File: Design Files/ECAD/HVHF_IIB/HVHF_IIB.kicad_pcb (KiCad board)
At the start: 2 copper layers, 36 parts, among them J1 1984963, J2 1984963, Q1 PNP, Q2 BFP196E6327HTSA1, T1 BFU590G, T1 NPN

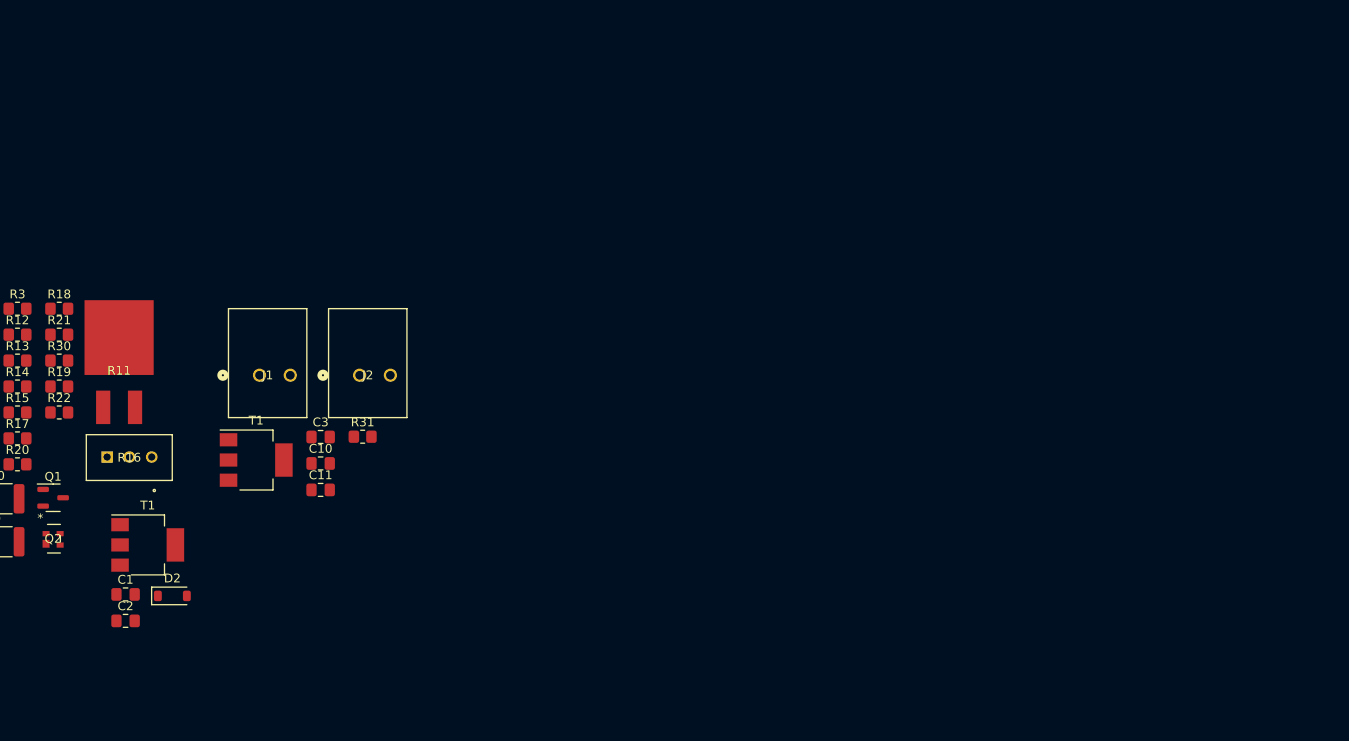
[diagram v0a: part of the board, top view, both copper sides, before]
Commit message: adds footprints
3d models
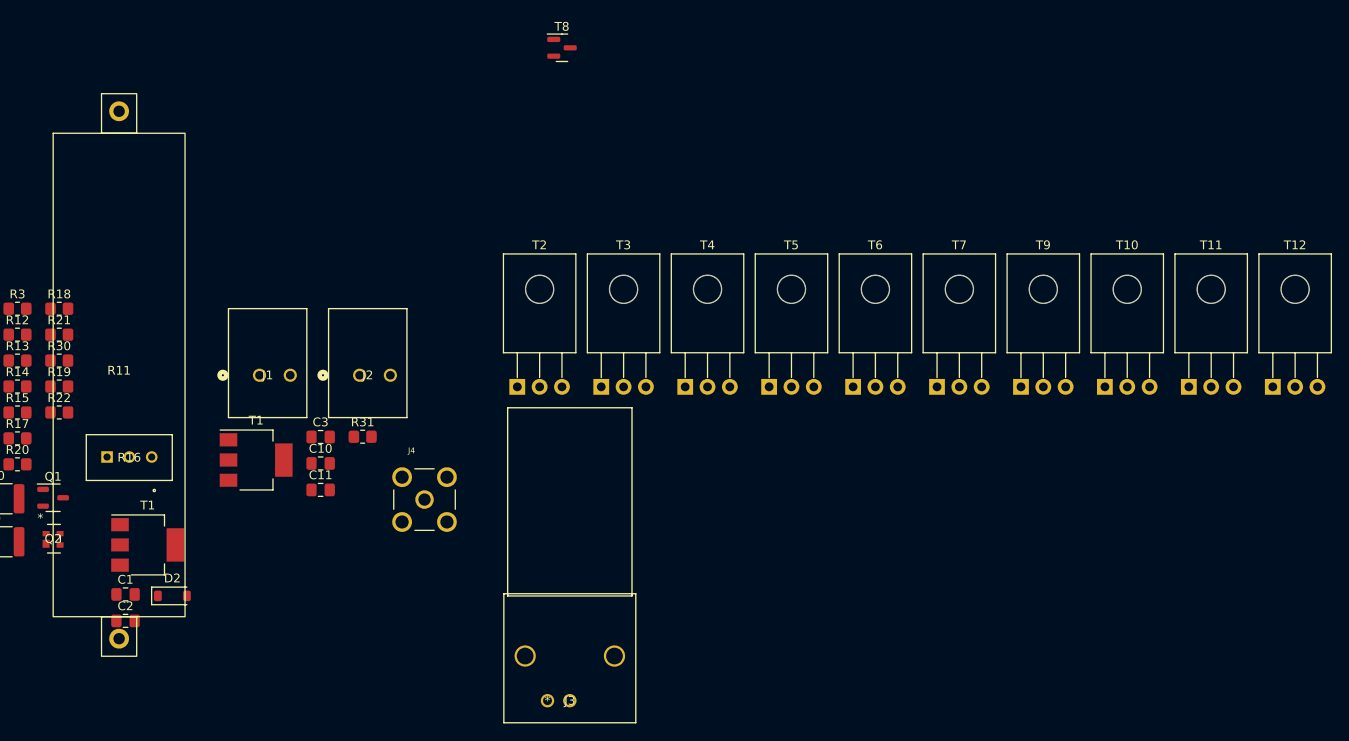
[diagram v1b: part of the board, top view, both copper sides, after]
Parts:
- added J3: 731375003, Library:CONN_73137-5003_MOL, F.Cu at (-298.4, 79.8)
- added J4: CONSMA002-L, Library:LINX_CONSMA002-L, F.Cu at (-314.9, 57.0)
- added T10: BFQ252, Package_TO_SOT_THT:TO-126-3_Horizontal_TabDown, F.Cu at (-237.5, 44.1)
- added T11: BFQ252, Package_TO_SOT_THT:TO-126-3_Horizontal_TabDown, F.Cu at (-228.0, 44.1)
- added T12: BFQ252, Package_TO_SOT_THT:TO-126-3_Horizontal_TabDown, F.Cu at (-218.4, 44.1)
- added T2: BFQ262, Package_TO_SOT_THT:TO-126-3_Horizontal_TabDown, F.Cu at (-304.4, 44.1)
- added T3: BFQ262, Package_TO_SOT_THT:TO-126-3_Horizontal_TabDown, F.Cu at (-294.8, 44.1)
- added T4: BFQ252, Package_TO_SOT_THT:TO-126-3_Horizontal_TabDown, F.Cu at (-285.3, 44.1)
- added T5: BFQ262, Package_TO_SOT_THT:TO-126-3_Horizontal_TabDown, F.Cu at (-275.7, 44.1)
- added T6: BFQ262, Package_TO_SOT_THT:TO-126-3_Horizontal_TabDown, F.Cu at (-266.2, 44.1)
- added T7: BFQ262, Package_TO_SOT_THT:TO-126-3_Horizontal_TabDown, F.Cu at (-256.6, 44.1)
- added T8: ~, Package_TO_SOT_SMD:SOT-23, F.Cu at (-299.3, 5.55)
- added T9: BFQ262, Package_TO_SOT_THT:TO-126-3_Horizontal_TabDown, F.Cu at (-247.1, 44.1)
- R11: footprint Library:PWR163 DPAK -> Library:PWWR0016
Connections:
- J1 pad 1: unconnected-(J1-Pad1) -> +VDC
- J1 pad 2: unconnected-(J1-Pad2) -> GND
- J2 pad 1: unconnected-(J2-Pad1) -> +5V
- J2 pad 2: unconnected-(J2-Pad2) -> GND

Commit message: wrapped up schematic
placed and routed all components on schematic
adds all footprints
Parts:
- added C4: C_Trim, Library:PPZC80003, F.Cu at (142.6, 96.2)
- added C5: 100u, Capacitor_SMD:C_1206_3216Metric_Pad1.33x1.80mm_HandSolder, F.Cu at (153.1, 107.9)
- added C6: 100u, Library:CAP_EEUED_125X25_PAN, F.Cu at (156.2, 99.0)
- added C7: 0.1u, Capacitor_SMD:C_1206_3216Metric_Pad1.33x1.80mm_HandSolder, F.Cu at (153.1, 111.2)
- added D1: BAT64, Library:CR_BAS70-02V_INF-L, F.Cu at (180.8, 104.0)
- added HS1: ~, Library:ATS_PCB1025, F.Cu at (201.8, 94.0)
- added HS10: ~, Library:ATS_PCB1025, F.Cu at (220.0, 127.0)
- added HS2: ~, Library:ATS_PCB1025, F.Cu at (201.8, 105.0)
- added HS3: ~, Library:ATS_PCB1025, F.Cu at (201.8, 116.2)
- added HS4: ~, Library:ATS_PCB1025, F.Cu at (201.8, 127.2)
- added HS5: ~, Library:ATS_PCB1025, F.Cu at (220.0, 71.5)
- added HS6: ~, Library:ATS_PCB1025, F.Cu at (220.0, 82.6)
- added HS7: ~, Library:ATS_PCB1025, F.Cu at (220.0, 93.7)
- added HS8: ~, Library:ATS_PCB1025, F.Cu at (220.0, 104.8)
- added HS9: ~, Library:ATS_PCB1025, F.Cu at (220.0, 115.9)
- moved C1 420.2 mm to (69.5, 105.7)
- moved C10 420.2 mm to (91.7, 90.8)
- moved C11 420.2 mm to (91.7, 93.8)
- moved C2 420.2 mm to (69.5, 108.8)
- moved C3 420.2 mm to (91.7, 87.8)
- moved D2 420.2 mm to (74.9, 105.9)
- moved J1 420.2 mm to (86.6, 80.8)
- moved J2 420.2 mm to (98.0, 80.8)
- moved J4 420.2 mm to (103.5, 95.0)
- moved Q1 420.2 mm to (61.3, 94.7)
- moved Q2 420.2 mm to (61.3, 99.4)
- moved R1 420.2 mm to (52.5, 73.2)
- moved R10 420.2 mm to (54.5, 94.9)
- moved R11 420.2 mm to (68.8, 80.8)
- moved R12 420.2 mm to (57.2, 76.2)
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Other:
- board outline added: 200 x 100 mm

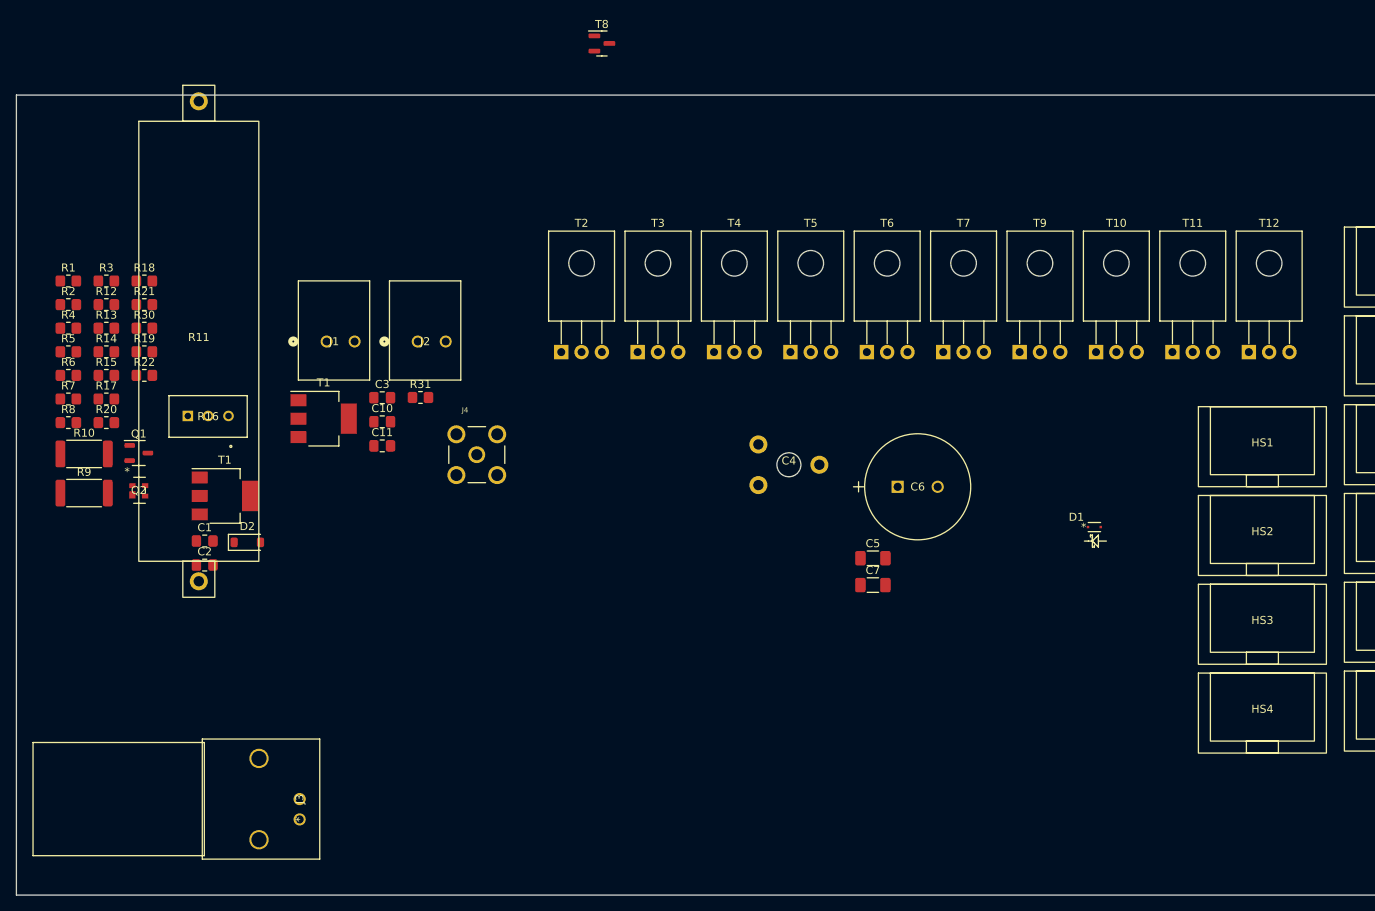
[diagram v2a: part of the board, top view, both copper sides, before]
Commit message: PCB layout
adds bard logo
began pcb layout
adds 3D model heat sink
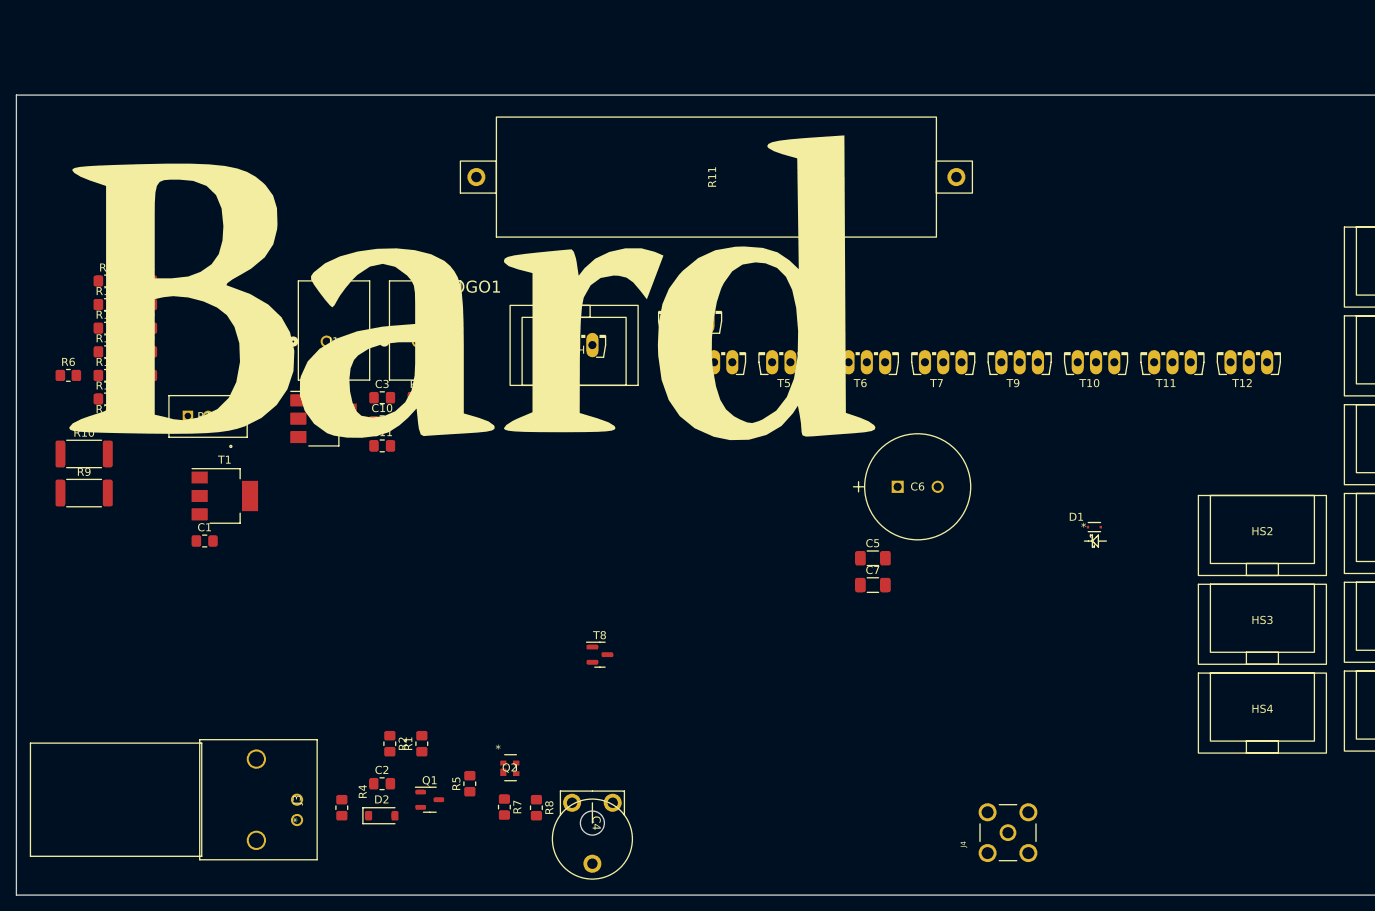
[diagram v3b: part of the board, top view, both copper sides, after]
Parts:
- added LOGO1: ~, Library:Bard_Logo, F.Cu at (103.0, 74.0)
- T10, T11, T12, T2, T3, T4, T5, T6, T7, T9: footprint Package_TO_SOT_THT:TO-126-3_Horizontal_TabDown -> Library:TO126AV
- moved HS1 87.0 mm to (115.7, 81.3), turned to 180 degrees
- moved J4 81.5 mm to (169.9, 142.2), turned to 90 degrees
- moved T8 76.4 mm to (118.9, 120.0)
- moved R8 75.8 mm to (111.0, 139.1), turned to -90 degrees
- moved R7 74.7 mm to (107.0, 139.0), turned to -90 degrees
- moved R5 73.7 mm to (102.7, 136.1), turned to 90 degrees
- moved R1 72.8 mm to (96.7, 131.1), turned to 90 degrees
- moved R4 69.0 mm to (86.7, 139.1), turned to -90 degrees
- moved R2 68.0 mm to (92.7, 131.1), turned to -90 degrees
- moved R11 67.9 mm to (133.5, 60.2), turned to 90 degrees
- moved Q2 57.9 mm to (107.7, 134.1)
- moved Q1 56.6 mm to (97.7, 138.1)
- moved C4 51.1 mm to (118.0, 141.0), turned to -90 degrees
- moved D2 38.1 mm to (91.7, 140.1)
- moved C2 35.2 mm to (91.7, 136.1)
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
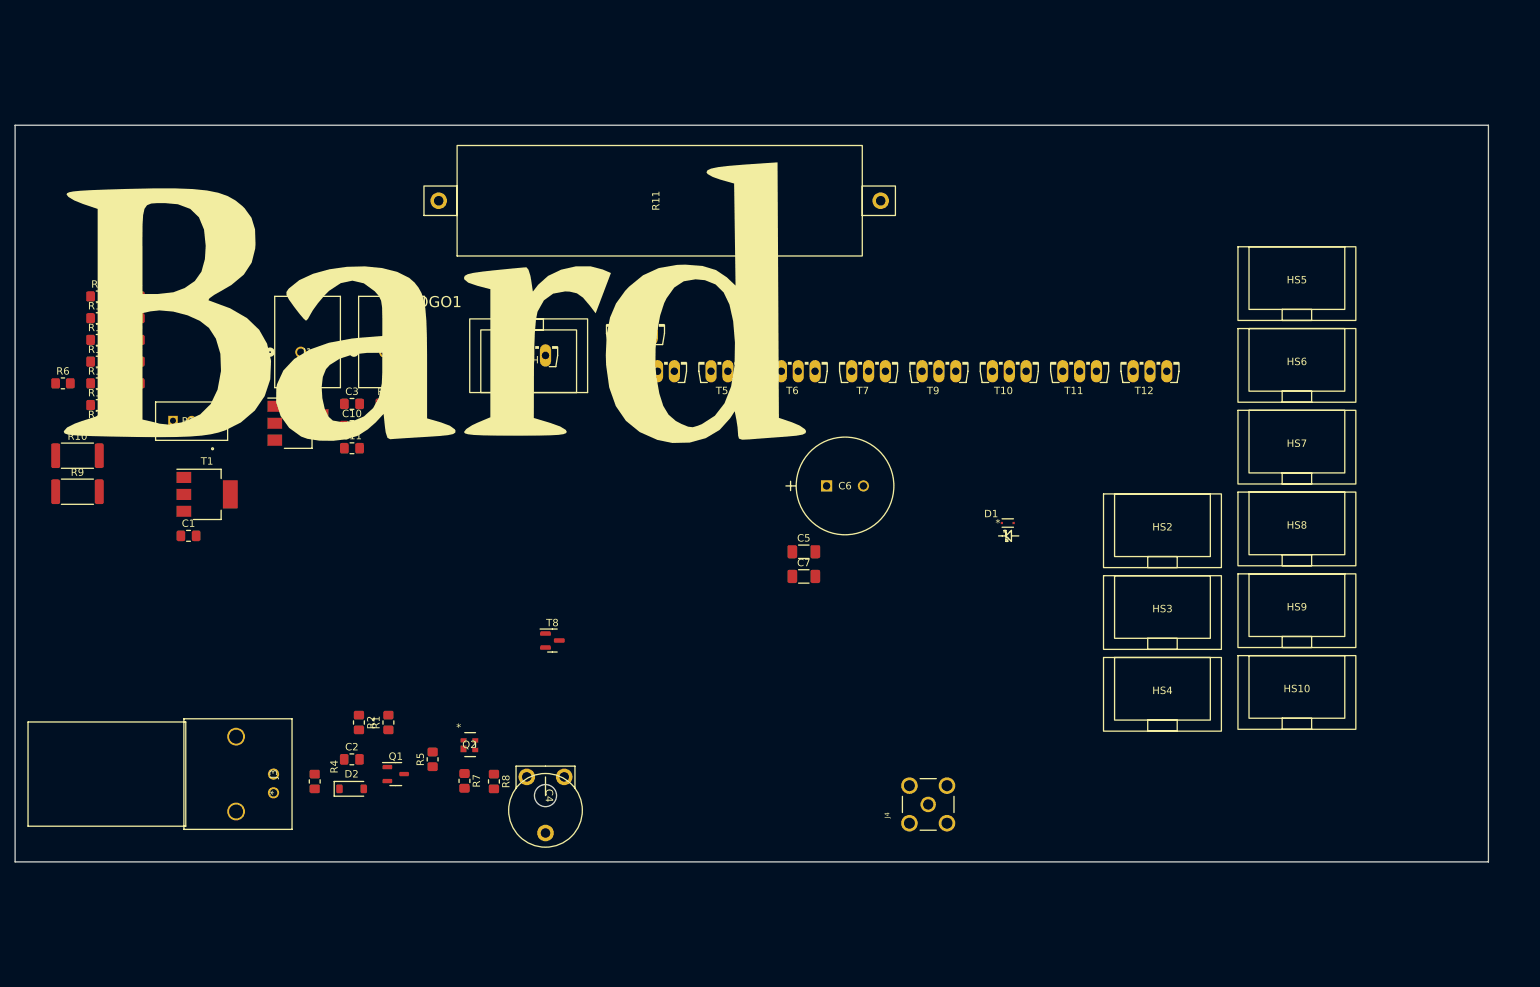
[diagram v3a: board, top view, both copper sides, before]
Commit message: board layout
sourced all components
laid out all components
designed all 3D models
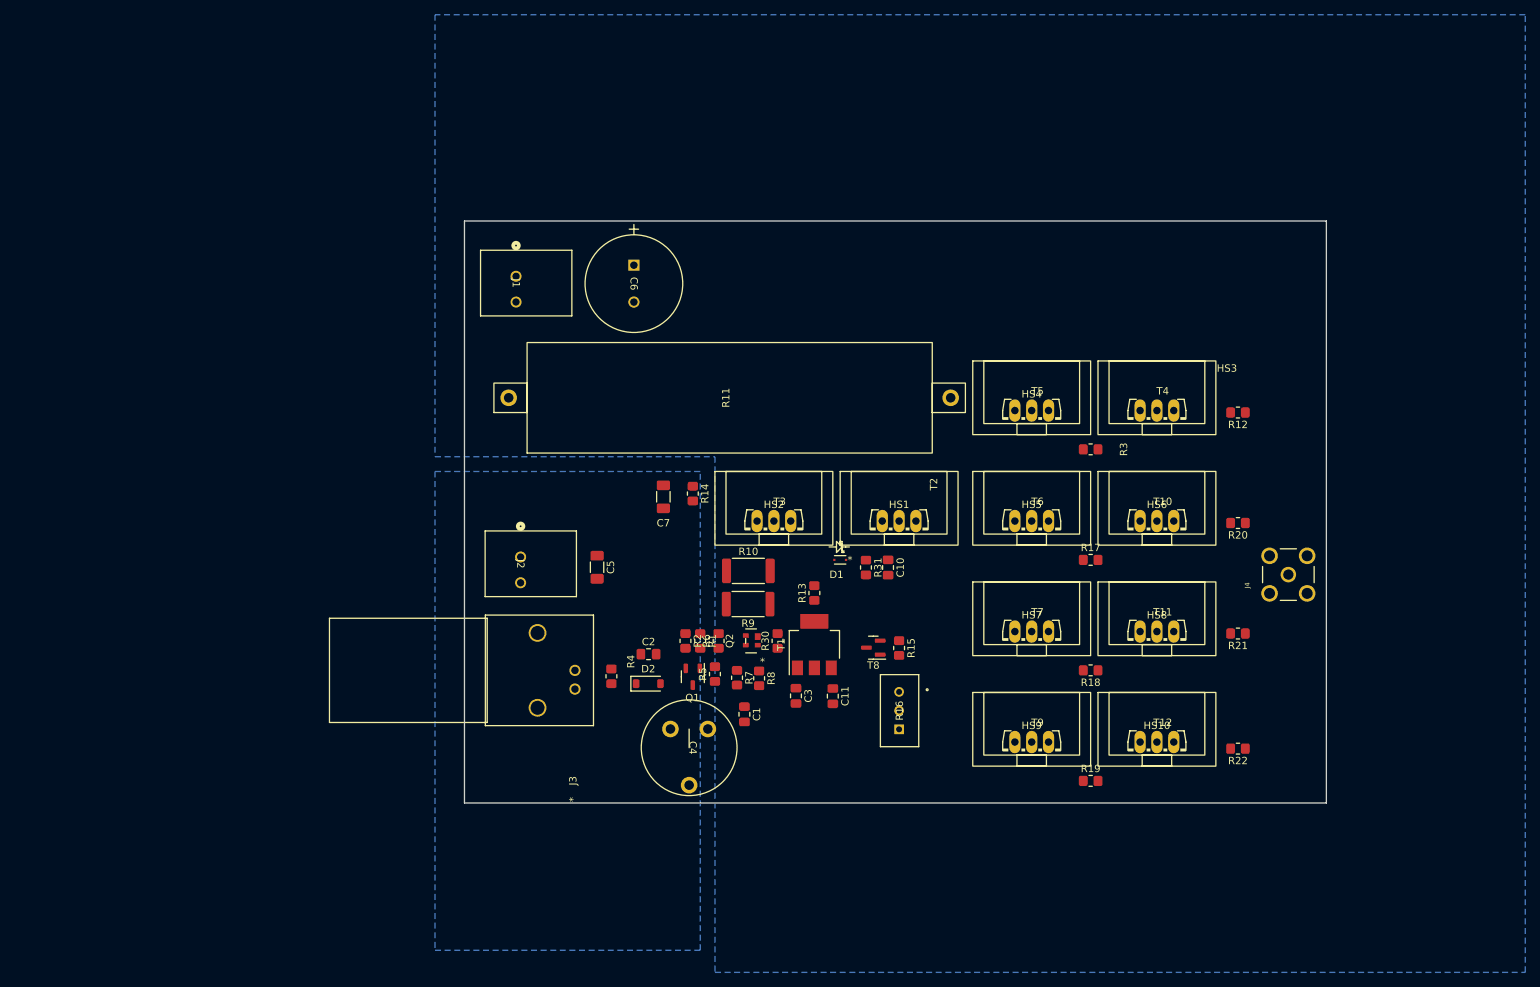
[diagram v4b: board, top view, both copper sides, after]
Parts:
- removed the T1 at (84.4, 90.5)
- removed the T1 at (72.1, 100.1)
- added T1: BFU590G, Package_TO_SOT_SMD:SOT-223, F.Cu at (154.5, 120.5)
- LOGO1: moved to B.Cu
- moved R22 158.0 mm to (212.0, 134.6), turned to 180 degrees
- moved R21 156.0 mm to (212.0, 119.0), turned to 180 degrees
- moved R20 155.3 mm to (212.0, 104.0), turned to 180 degrees
- moved R12 155.3 mm to (212.0, 89.0), turned to 180 degrees
- moved R19 141.9 mm to (192.0, 139.0)
- moved R18 139.6 mm to (192.0, 124.0), turned to 180 degrees
- moved R17 136.4 mm to (192.0, 109.0)
- moved R3 136.3 mm to (192.0, 94.0)
- moved R15 114.5 mm to (166.0, 121.0), turned to -90 degrees
- moved R16 107.1 mm to (166.0, 132.0), turned to 90 degrees
- moved R13 103.1 mm to (154.5, 113.5), turned to 90 degrees
- moved R30 96.6 mm to (149.5, 120.0), turned to 90 degrees
- moved R6 95.6 mm to (141.5, 120.0), turned to 90 degrees
- moved R10 92.4 mm to (145.5, 110.5)
- moved R9 92.3 mm to (145.5, 115.0), turned to 180 degrees
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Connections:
- net Net-(D1-A) renamed /FB1
- net Net-(Q2-C) renamed /FB2
- C10 pad 1: +5V -> Net-(T2-B)
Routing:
- added copper zone on B.Cu, net +5V
- added copper zone on B.Cu, net +VDC
- added copper zone on In1.Cu, net GND
- added copper zone on In2.Cu, net GND
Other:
- board size 200 x 100 mm -> 117 x 79 mm
- copper layers 2 -> 4
